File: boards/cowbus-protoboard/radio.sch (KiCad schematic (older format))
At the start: 3 parts

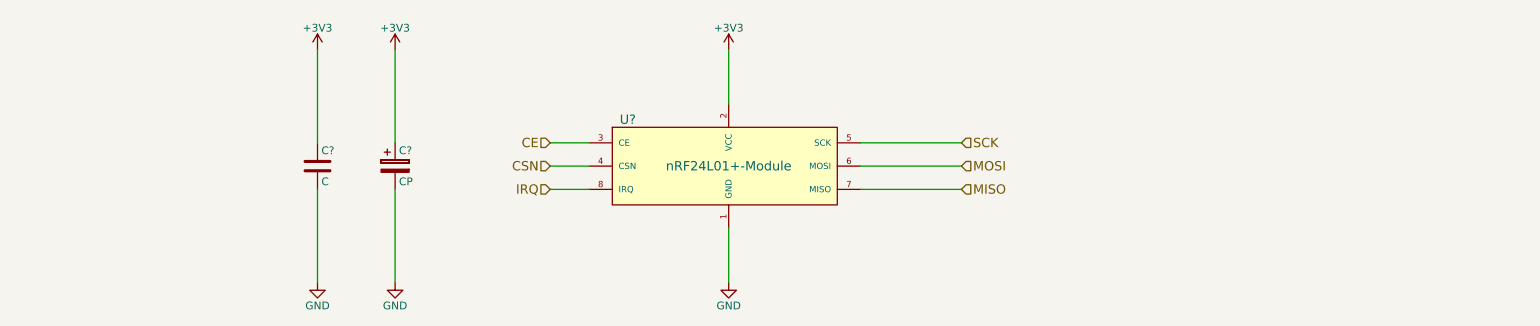
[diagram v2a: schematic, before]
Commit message: values added, 100n for uC added
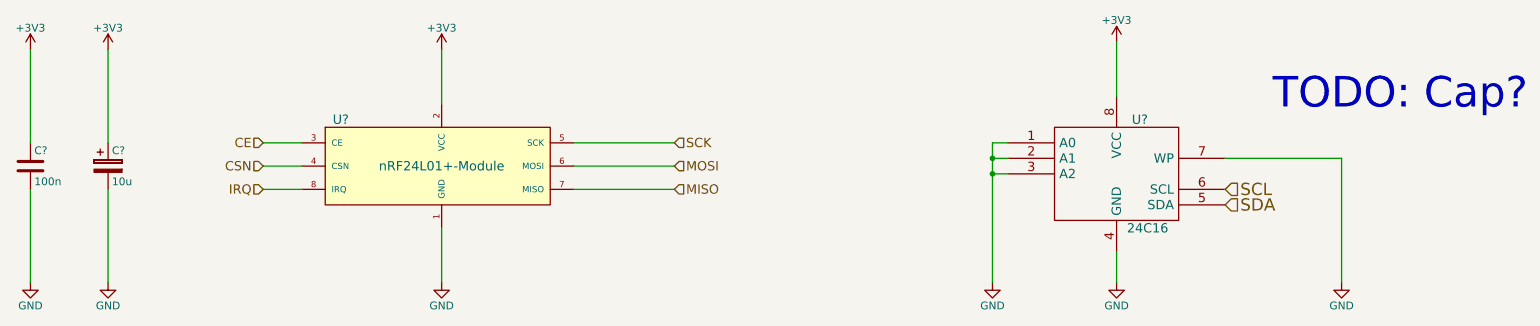
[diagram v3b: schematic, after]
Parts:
- added U?: 24C16, symbol 24C16
- C?: value C -> 100n
- C?: value CP -> 10u
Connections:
- net +3V3: now also U?.8 (VCC)
- net GND: now also U?.1 (A0), U?.2 (A1), U?.3 (A2), U?.4 (GND), U?.7 (WP)
- new net SCL: U?.6 (SCL)
- new net SDA: U?.5 (SDA)
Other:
- note added: "TODO: Cap?"
- moved on the sheet: C?, U?
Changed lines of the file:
@@
 encoding utf-8
 Sheet 4 6
-Title ""
-Date ""
-Rev ""
+Title "cowbus protoboard"
+Date "2015-07-15"
+Rev "0.9"
 Comp ""
 Comment1 ""
@@
 L nRF24L01+-Module U?
 U 1 1 55A51C3D
-P 5650 3950
-F 0 "U?" H 5000 4250 60  0000 C CNN
-F 1 "nRF24L01+-Module" H 5650 3950 60  0000 C CNN
-F 2 "" H 5750 3550 60  0000 C CNN
-F 3 "" H 5750 3550 60  0000 C CNN
-	1    5650 3950
+P 3800 3950
+F 0 "U?" H 3150 4250 60  0000 C CNN
+F 1 "nRF24L01+-Module" H 3800 3950 60  0000 C CNN
+F 2 "" H 3900 3550 60  0000 C CNN
+F 3 "" H 3900 3550 60  0000 C CNN
+	1    3800 3950
 	1    0    0    -1
 $EndComp
@@
 L GND #PWR?
 U 1 1 55A51C67
-P 5650 4700
-F 0 "#PWR?" H 5650 4450 50  0001 C CNN
-F 1 "GND" H 5650 4550 50  0000 C CNN
-F 2 "" H 5650 4700 60  0000 C CNN
-F 3 "" H 5650 4700 60  0000 C CNN
-	1    5650 4700
+P 3800 4700
+F 0 "#PWR?" H 3800 4450 50  0001 C CNN
+F 1 "GND" H 3800 4550 50  0000 C CNN
+F 2 "" H 3800 4700 60  0000 C CNN
+F 3 "" H 3800 4700 60  0000 C CNN
+	1    3800 4700
 	1    0    0    -1
 $EndComp
@@
 L +3V3 #PWR?
 U 1 1 55A51C7D
-P 5650 3200
-F 0 "#PWR?" H 5650 3050 50  0001 C CNN
-F 1 "+3V3" H 5650 3340 50  0000 C CNN
-F 2 "" H 5650 3200 60  0000 C CNN
-F 3 "" H 5650 3200 60  0000 C CNN
-	1    5650 3200
-	1    0    0    -1
-$EndComp
-Text HLabel 7150 3800 2    60   Input ~ 0
+P 3800 3200
+F 0 "#PWR?" H 3800 3050 50  0001 C CNN
+F 1 "+3V3" H 3800 3340 50  0000 C CNN
+F 2 "" H 3800 3200 60  0000 C CNN
+F 3 "" H 3800 3200 60  0000 C CNN
+	1    3800 3200
+	1    0    0    -1
+$EndComp
+Text HLabel 5300 3800 2    60   Input ~ 0
 SCK
 Wire Wire Line
-	5650 3550 5650 3200
-Wire Wire Line
-	5650 4350 5650 4700
-Wire Wire Line
-	6500 3800 7150 3800
-Wire Wire Line
-	6500 3950 7150 3950
-Wire Wire Line
-	6500 4100 7150 4100
-Text HLabel 7150 3950 2    60   Input ~ 0
+	3800 3550 3800 3200
+Wire Wire Line
+	3800 4350 3800 4700
+Wire Wire Line
+	4650 3800 5300 3800
+Wire Wire Line
+	4650 3950 5300 3950
+Wire Wire Line
+	4650 4100 5300 4100
+Text HLabel 5300 3950 2    60   Input ~ 0
 MOSI
-Text HLabel 7150 4100 2    60   Input ~ 0
+Text HLabel 5300 4100 2    60   Input ~ 0
 MISO
 Wire Wire Line
-	4750 3800 4500 3800
-Wire Wire Line
-	4750 3950 4500 3950
-Wire Wire Line
-	4750 4100 4500 4100
-Text HLabel 4500 3800 0    60   Input ~ 0
+	2900 3800 2650 3800
+Wire Wire Line
+	2900 3950 2650 3950
+Wire Wire Line
+	2900 4100 2650 4100
+Text HLabel 2650 3800 0    60   Input ~ 0
 CE
-Text HLabel 4500 3950 0    60   Input ~ 0
+Text HLabel 2650 3950 0    60   Input ~ 0
 CSN
-Text HLabel 4500 4100 0    60   Input ~ 0
+Text HLabel 2650 4100 0    60   Input ~ 0
 IRQ
 $Comp
 L GND #PWR?
 U 1 1 55A72AEE
-P 3000 4700
-F 0 "#PWR?" H 3000 4450 50  0001 C CNN
-F 1 "GND" H 3000 4550 50  0000 C CNN
-F 2 "" H 3000 4700 60  0000 C CNN
-F 3 "" H 3000 4700 60  0000 C CNN
-	1    3000 4700
+P 1150 4700
+F 0 "#PWR?" H 1150 4450 50  0001 C CNN
+F 1 "GND" H 1150 4550 50  0000 C CNN
+F 2 "" H 1150 4700 60  0000 C CNN
+F 3 "" H 1150 4700 60  0000 C CNN
+	1    1150 4700
 	1    0    0    -1
 $EndComp
@@
 L +3V3 #PWR?
 U 1 1 55A72AF4
-P 3000 3200
-F 0 "#PWR?" H 3000 3050 50  0001 C CNN
-F 1 "+3V3" H 3000 3340 50  0000 C CNN
-F 2 "" H 3000 3200 60  0000 C CNN
-F 3 "" H 3000 3200 60  0000 C CNN
-	1    3000 3200
-	1    0    0    -1
-$EndComp
-Wire Wire Line
-	3000 3200 3000 3800
-Wire Wire Line
-	3000 4100 3000 4700
+P 1150 3200
+F 0 "#PWR?" H 1150 3050 50  0001 C CNN
+F 1 "+3V3" H 1150 3340 50  0000 C CNN
+F 2 "" H 1150 3200 60  0000 C CNN
+F 3 "" H 1150 3200 60  0000 C CNN
+	1    1150 3200
+	1    0    0    -1
+$EndComp
+Wire Wire Line
+	1150 3200 1150 3800
+Wire Wire Line
+	1150 4100 1150 4700
 $Comp
 L C C?
 U 1 1 55A72B04
-P 3000 3950
-F 0 "C?" H 3025 4050 50  0000 L CNN
-F 1 "C" H 3025 3850 50  0000 L CNN
-F 2 "" H 3038 3800 30  0000 C CNN
-F 3 "" H 3000 3950 60  0000 C CNN
-	1    3000 3950
+P 1150 3950
+F 0 "C?" H 1175 4050 50  0000 L CNN
+F 1 "100n" H 1175 3850 50  0000 L CNN
+F 2 "" H 1188 3800 30  0000 C CNN
+F 3 "" H 1150 3950 60  0000 C CNN
+	1    1150 3950
 	1    0    0    -1
 $EndComp
@@
 L CP C?
 U 1 1 55A72B51
-P 3500 3950
-F 0 "C?" H 3525 4050 50  0000 L CNN
-F 1 "CP" H 3525 3850 50  0000 L CNN
-F 2 "" H 3538 3800 30  0000 C CNN
-F 3 "" H 3500 3950 60  0000 C CNN
-	1    3500 3950
-	1    0    0    -1
-$EndComp
-Wire Wire Line
-	3500 3800 3500 3200
-Wire Wire Line
-	3500 4100 3500 4700
+P 1650 3950
+F 0 "C?" H 1675 4050 50  0000 L CNN
+F 1 "10u" H 1675 3850 50  0000 L CNN
+F 2 "" H 1688 3800 30  0000 C CNN
+F 3 "" H 1650 3950 60  0000 C CNN
+	1    1650 3950
+	1    0    0    -1
+$EndComp
+Wire Wire Line
+	1650 3800 1650 3200
+Wire Wire Line
+	1650 4100 1650 4700
 $Comp
 L GND #PWR?
 U 1 1 55A72BFA
-P 3500 4700
-F 0 "#PWR?" H 3500 4450 50  0001 C CNN
-F 1 "GND" H 3500 4550 50  0000 C CNN
-F 2 "" H 3500 4700 60  0000 C CNN
-F 3 "" H 3500 4700 60  0000 C CNN
-	1    3500 4700
+P 1650 4700
+F 0 "#PWR?" H 1650 4450 50  0001 C CNN
+F 1 "GND" H 1650 4550 50  0000 C CNN
+F 2 "" H 1650 4700 60  0000 C CNN
+F 3 "" H 1650 4700 60  0000 C CNN
+	1    1650 4700
 	1    0    0    -1
 $EndComp
@@
 L +3V3 #PWR?
 U 1 1 55A72C0E
-P 3500 3200
-F 0 "#PWR?" H 3500 3050 50  0001 C CNN
-F 1 "+3V3" H 3500 3340 50  0000 C CNN
-F 2 "" H 3500 3200 60  0000 C CNN
-F 3 "" H 3500 3200 60  0000 C CNN
-	1    3500 3200
-	1    0    0    -1
-$EndComp
+P 1650 3200
+F 0 "#PWR?" H 1650 3050 50  0001 C CNN
+F 1 "+3V3" H 1650 3340 50  0000 C CNN
+F 2 "" H 1650 3200 60  0000 C CNN
+F 3 "" H 1650 3200 60  0000 C CNN
+	1    1650 3200
+	1    0    0    -1
+$EndComp
+$Comp
+L 24C16 U?
+U 1 1 55A89592
+P 8150 4000
+F 0 "U?" H 8300 4350 60  0000 C CNN
+F 1 "24C16" H 8350 3650 60  0000 C CNN
+F 2 "" H 8150 4000 60  0000 C CNN
+F 3 "" H 8150 4000 60  0000 C CNN
+	1    8150 4000
+	1    0    0    -1
+$EndComp
+$Comp
+L +3V3 #PWR?
+U 1 1 55A89652
+P 8150 3150
+F 0 "#PWR?" H 8150 3000 50  0001 C CNN
+F 1 "+3V3" H 8150 3290 50  0000 C CNN
+F 2 "" H 8150 3150 60  0000 C CNN
+F 3 "" H 8150 3150 60  0000 C CNN
+	1    8150 3150
+	1    0    0    -1
+$EndComp
+Wire Wire Line
+	8150 3500 8150 3150
+$Comp
+L GND #PWR?
+U 1 1 55A89738
+P 8150 4700
+F 0 "#PWR?" H 8150 4450 50  0001 C CNN
+F 1 "GND" H 8150 4550 50  0000 C CNN
+F 2 "" H 8150 4700 60  0000 C CNN
+F 3 "" H 8150 4700 60  0000 C CNN
+	1    8150 4700
+	1    0    0    -1
+$EndComp
+Wire Wire Line
+	8150 4700 8150 4500
+Wire Wire Line
+	7450 3800 7350 3800
+Wire Wire Line
+	7350 3800 7350 4700
+Wire Wire Line
+	7450 3900 7350 3900
+Connection ~ 7350 3900
+Wire Wire Line
+	7450 4000 7350 4000
+Connection ~ 7350 4000
+$Comp
+L GND #PWR?
+U 1 1 55A89845
+P 7350 4700
+F 0 "#PWR?" H 7350 4450 50  0001 C CNN
+F 1 "GND" H 7350 4550 50  0000 C CNN
+F 2 "" H 7350 4700 60  0000 C CNN
+F 3 "" H 7350 4700 60  0000 C CNN
+	1    7350 4700
+	1    0    0    -1
+$EndComp
+Wire Wire Line
+	8850 3900 9600 3900
+$Comp
+L GND #PWR?
+U 1 1 55A8993F
+P 9600 4700
+F 0 "#PWR?" H 9600 4450 50  0001 C CNN
+F 1 "GND" H 9600 4550 50  0000 C CNN
+F 2 "" H 9600 4700 60  0000 C CNN
+F 3 "" H 9600 4700 60  0000 C CNN
+	1    9600 4700
+	1    0    0    -1
+$EndComp
+Wire Wire Line
+	9600 3900 9600 4700
+Text HLabel 8850 4100 2    79   Input ~ 0
+SCL
+Text HLabel 8850 4200 2    79   Input ~ 0
+SDA
+Text Notes 10800 3600 2    197  ~ 0
+TODO: Cap?
 $EndSCHEMATC

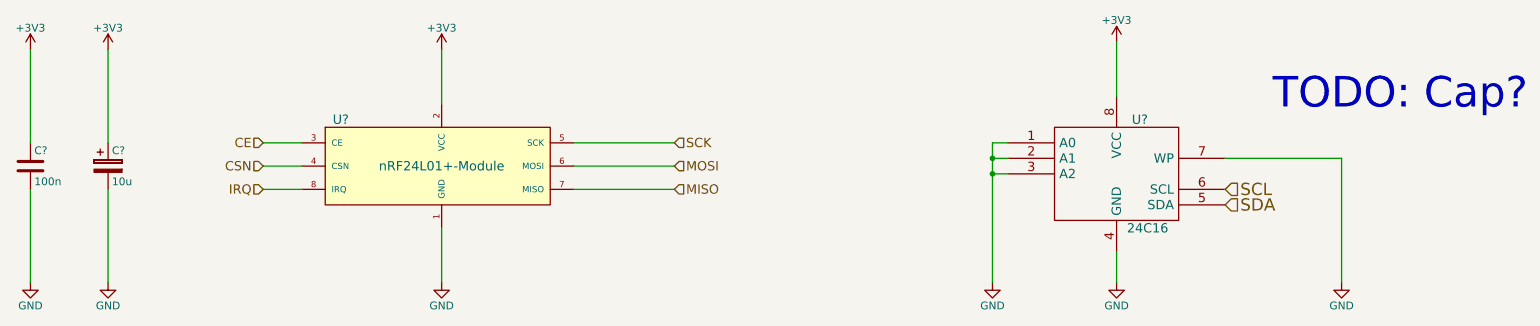
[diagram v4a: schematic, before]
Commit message: some footprint assignments done
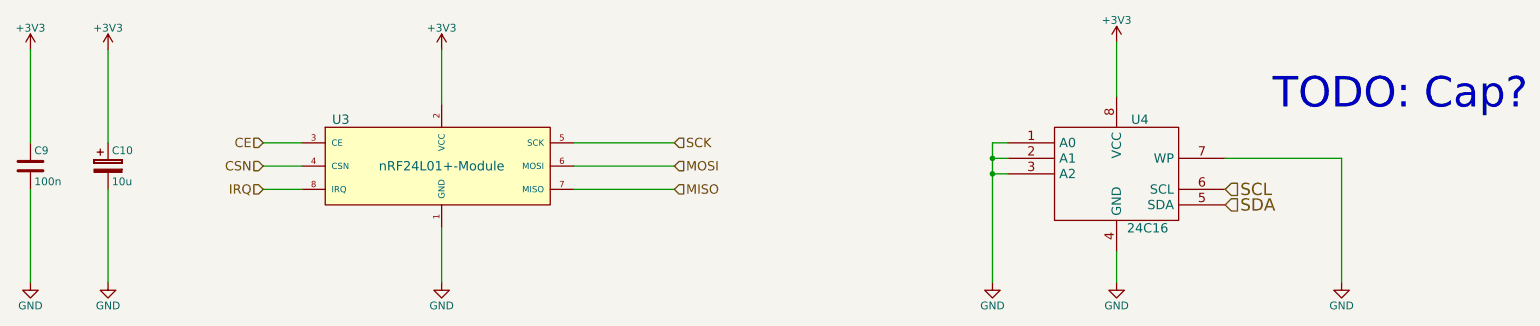
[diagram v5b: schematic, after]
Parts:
- C10: renamed from C?; footprint (none) -> Capacitors_SMD:c_elec_4x5.8
- C9: renamed from C?; footprint (none) -> Capacitors_SMD:C_0805_HandSoldering
- U3: renamed from U?; footprint (none) -> Pin_Headers:Pin_Header_Straight_2x05
- gave numbers to parts that had none: 1
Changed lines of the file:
@@
 $EndDescr
 $Comp
-L nRF24L01+-Module U?
+L nRF24L01+-Module U3
 U 1 1 55A51C3D
 P 3800 3950
-F 0 "U?" H 3150 4250 60  0000 C CNN
+F 0 "U3" H 3150 4250 60  0000 C CNN
 F 1 "nRF24L01+-Module" H 3800 3950 60  0000 C CNN
-F 2 "" H 3900 3550 60  0000 C CNN
+F 2 "Pin_Headers:Pin_Header_Straight_2x05" H 3900 3550 60  0001 C CNN
 F 3 "" H 3900 3550 60  0000 C CNN
 	1    3800 3950
@@
 $EndComp
 $Comp
-L GND #PWR?
+L GND #PWR031
 U 1 1 55A51C67
 P 3800 4700
-F 0 "#PWR?" H 3800 4450 50  0001 C CNN
+F 0 "#PWR031" H 3800 4450 50  0001 C CNN
 F 1 "GND" H 3800 4550 50  0000 C CNN
 F 2 "" H 3800 4700 60  0000 C CNN
@@
 $EndComp
 $Comp
-L +3V3 #PWR?
+L +3V3 #PWR032
 U 1 1 55A51C7D
 P 3800 3200
-F 0 "#PWR?" H 3800 3050 50  0001 C CNN
+F 0 "#PWR032" H 3800 3050 50  0001 C CNN
 F 1 "+3V3" H 3800 3340 50  0000 C CNN
 F 2 "" H 3800 3200 60  0000 C CNN
@@
 IRQ
 $Comp
-L GND #PWR?
+L GND #PWR033
 U 1 1 55A72AEE
 P 1150 4700
-F 0 "#PWR?" H 1150 4450 50  0001 C CNN
+F 0 "#PWR033" H 1150 4450 50  0001 C CNN
 F 1 "GND" H 1150 4550 50  0000 C CNN
 F 2 "" H 1150 4700 60  0000 C CNN
@@
 $EndComp
 $Comp
-L +3V3 #PWR?
+L +3V3 #PWR034
 U 1 1 55A72AF4
 P 1150 3200
-F 0 "#PWR?" H 1150 3050 50  0001 C CNN
+F 0 "#PWR034" H 1150 3050 50  0001 C CNN
 F 1 "+3V3" H 1150 3340 50  0000 C CNN
 F 2 "" H 1150 3200 60  0000 C CNN
@@
 	1150 4100 1150 4700
 $Comp
-L C C?
+L C C9
 U 1 1 55A72B04
 P 1150 3950
-F 0 "C?" H 1175 4050 50  0000 L CNN
+F 0 "C9" H 1175 4050 50  0000 L CNN
 F 1 "100n" H 1175 3850 50  0000 L CNN
-F 2 "" H 1188 3800 30  0000 C CNN
+F 2 "Capacitors_SMD:C_0805_HandSoldering" H 1188 3800 30  0001 C CNN
 F 3 "" H 1150 3950 60  0000 C CNN
 	1    1150 3950
@@
 $EndComp
 $Comp
-L CP C?
+L CP C10
 U 1 1 55A72B51
 P 1650 3950
-F 0 "C?" H 1675 4050 50  0000 L CNN
+F 0 "C10" H 1675 4050 50  0000 L CNN
 F 1 "10u" H 1675 3850 50  0000 L CNN
-F 2 "" H 1688 3800 30  0000 C CNN
+F 2 "Capacitors_SMD:c_elec_4x5.8" H 1688 3800 30  0001 C CNN
 F 3 "" H 1650 3950 60  0000 C CNN
 	1    1650 3950
@@
 	1650 4100 1650 4700
 $Comp
-L GND #PWR?
+L GND #PWR035
 U 1 1 55A72BFA
 P 1650 4700
-F 0 "#PWR?" H 1650 4450 50  0001 C CNN
+F 0 "#PWR035" H 1650 4450 50  0001 C CNN
 F 1 "GND" H 1650 4550 50  0000 C CNN
 F 2 "" H 1650 4700 60  0000 C CNN
@@
 $EndComp
 $Comp
-L +3V3 #PWR?
+L +3V3 #PWR036
 U 1 1 55A72C0E
 P 1650 3200
-F 0 "#PWR?" H 1650 3050 50  0001 C CNN
+F 0 "#PWR036" H 1650 3050 50  0001 C CNN
 F 1 "+3V3" H 1650 3340 50  0000 C CNN
 F 2 "" H 1650 3200 60  0000 C CNN
@@
 $EndComp
 $Comp
-L 24C16 U?
+L 24C16 U4
 U 1 1 55A89592
 P 8150 4000
-F 0 "U?" H 8300 4350 60  0000 C CNN
+F 0 "U4" H 8300 4350 60  0000 C CNN
 F 1 "24C16" H 8350 3650 60  0000 C CNN
-F 2 "" H 8150 4000 60  0000 C CNN
+F 2 "" H 8150 4000 60  0001 C CNN
 F 3 "" H 8150 4000 60  0000 C CNN
 	1    8150 4000
@@
 $EndComp
 $Comp
-L +3V3 #PWR?
+L +3V3 #PWR037
 U 1 1 55A89652
 P 8150 3150
-F 0 "#PWR?" H 8150 3000 50  0001 C CNN
+F 0 "#PWR037" H 8150 3000 50  0001 C CNN
 F 1 "+3V3" H 8150 3290 50  0000 C CNN
 F 2 "" H 8150 3150 60  0000 C CNN
@@
 	8150 3500 8150 3150
 $Comp
-L GND #PWR?
+L GND #PWR038
 U 1 1 55A89738
 P 8150 4700
-F 0 "#PWR?" H 8150 4450 50  0001 C CNN
+F 0 "#PWR038" H 8150 4450 50  0001 C CNN
 F 1 "GND" H 8150 4550 50  0000 C CNN
 F 2 "" H 8150 4700 60  0000 C CNN
@@
 Connection ~ 7350 4000
 $Comp
-L GND #PWR?
+L GND #PWR039
 U 1 1 55A89845
 P 7350 4700
-F 0 "#PWR?" H 7350 4450 50  0001 C CNN
+F 0 "#PWR039" H 7350 4450 50  0001 C CNN
 F 1 "GND" H 7350 4550 50  0000 C CNN
 F 2 "" H 7350 4700 60  0000 C CNN
@@
 	8850 3900 9600 3900
 $Comp
-L GND #PWR?
+L GND #PWR040
 U 1 1 55A8993F
 P 9600 4700
-F 0 "#PWR?" H 9600 4450 50  0001 C CNN
+F 0 "#PWR040" H 9600 4450 50  0001 C CNN
 F 1 "GND" H 9600 4550 50  0000 C CNN
 F 2 "" H 9600 4700 60  0000 C CNN

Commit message: first version of layout for protoboard
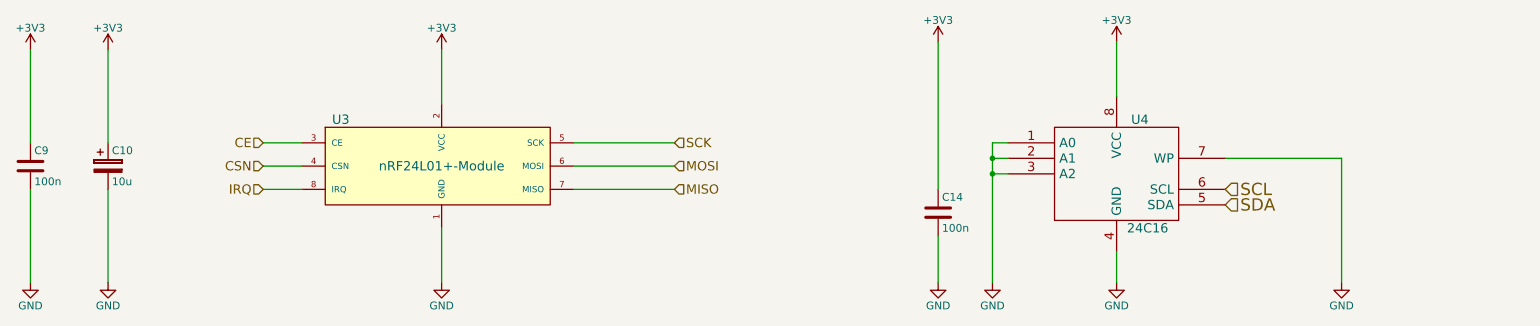
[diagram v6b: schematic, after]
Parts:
- added C14: 100n, Capacitors_SMD:C_0805_HandSoldering, symbol C
- U4: footprint (none) -> SMD_Packages:SOIC-8-N
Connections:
- net +3V3: now also C14.1
- net GND: now also C14.2
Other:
- note removed: "TODO: Cap?"
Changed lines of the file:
@@
 EESchema Schematic File Version 2
+LIBS:cowbus-protoboard-rescue
 LIBS:power
 LIBS:device
@@
 LIBS:nrf24l01plus-module
 LIBS:i2c
+LIBS:led_rgb_reichelt
 LIBS:cowbus-protoboard-cache
 EELAYER 25 0
@@
 $EndComp
 $Comp
-L GND #PWR031
+L GND #PWR43
 U 1 1 55A51C67
 P 3800 4700
-F 0 "#PWR031" H 3800 4450 50  0001 C CNN
+F 0 "#PWR43" H 3800 4450 50  0001 C CNN
 F 1 "GND" H 3800 4550 50  0000 C CNN
 F 2 "" H 3800 4700 60  0000 C CNN
@@
 $EndComp
 $Comp
-L +3V3 #PWR032
+L +3V3 #PWR42
 U 1 1 55A51C7D
 P 3800 3200
-F 0 "#PWR032" H 3800 3050 50  0001 C CNN
+F 0 "#PWR42" H 3800 3050 50  0001 C CNN
 F 1 "+3V3" H 3800 3340 50  0000 C CNN
 F 2 "" H 3800 3200 60  0000 C CNN
@@
 IRQ
 $Comp
-L GND #PWR033
+L GND #PWR39
 U 1 1 55A72AEE
 P 1150 4700
-F 0 "#PWR033" H 1150 4450 50  0001 C CNN
+F 0 "#PWR39" H 1150 4450 50  0001 C CNN
 F 1 "GND" H 1150 4550 50  0000 C CNN
 F 2 "" H 1150 4700 60  0000 C CNN
@@
 $EndComp
 $Comp
-L +3V3 #PWR034
+L +3V3 #PWR38
 U 1 1 55A72AF4
 P 1150 3200
-F 0 "#PWR034" H 1150 3050 50  0001 C CNN
+F 0 "#PWR38" H 1150 3050 50  0001 C CNN
 F 1 "+3V3" H 1150 3340 50  0000 C CNN
 F 2 "" H 1150 3200 60  0000 C CNN
@@
 	1650 4100 1650 4700
 $Comp
-L GND #PWR035
+L GND #PWR41
 U 1 1 55A72BFA
 P 1650 4700
-F 0 "#PWR035" H 1650 4450 50  0001 C CNN
+F 0 "#PWR41" H 1650 4450 50  0001 C CNN
 F 1 "GND" H 1650 4550 50  0000 C CNN
 F 2 "" H 1650 4700 60  0000 C CNN
@@
 $EndComp
 $Comp
-L +3V3 #PWR036
+L +3V3 #PWR40
 U 1 1 55A72C0E
 P 1650 3200
-F 0 "#PWR036" H 1650 3050 50  0001 C CNN
+F 0 "#PWR40" H 1650 3050 50  0001 C CNN
 F 1 "+3V3" H 1650 3340 50  0000 C CNN
 F 2 "" H 1650 3200 60  0000 C CNN
@@
 F 0 "U4" H 8300 4350 60  0000 C CNN
 F 1 "24C16" H 8350 3650 60  0000 C CNN
-F 2 "" H 8150 4000 60  0001 C CNN
+F 2 "SMD_Packages:SOIC-8-N" H 8150 4000 60  0001 C CNN
 F 3 "" H 8150 4000 60  0000 C CNN
 	1    8150 4000
@@
 $EndComp
 $Comp
-L +3V3 #PWR037
+L +3V3 #PWR47
 U 1 1 55A89652
 P 8150 3150
-F 0 "#PWR037" H 8150 3000 50  0001 C CNN
+F 0 "#PWR47" H 8150 3000 50  0001 C CNN
 F 1 "+3V3" H 8150 3290 50  0000 C CNN
 F 2 "" H 8150 3150 60  0000 C CNN
@@
 	8150 3500 8150 3150
 $Comp
-L GND #PWR038
+L GND #PWR48
 U 1 1 55A89738
 P 8150 4700
-F 0 "#PWR038" H 8150 4450 50  0001 C CNN
+F 0 "#PWR48" H 8150 4450 50  0001 C CNN
 F 1 "GND" H 8150 4550 50  0000 C CNN
 F 2 "" H 8150 4700 60  0000 C CNN
@@
 Connection ~ 7350 4000
 $Comp
-L GND #PWR039
+L GND #PWR46
 U 1 1 55A89845
 P 7350 4700
-F 0 "#PWR039" H 7350 4450 50  0001 C CNN
+F 0 "#PWR46" H 7350 4450 50  0001 C CNN
 F 1 "GND" H 7350 4550 50  0000 C CNN
 F 2 "" H 7350 4700 60  0000 C CNN
@@
 	8850 3900 9600 3900
 $Comp
-L GND #PWR040
+L GND #PWR49
 U 1 1 55A8993F
 P 9600 4700
-F 0 "#PWR040" H 9600 4450 50  0001 C CNN
+F 0 "#PWR49" H 9600 4450 50  0001 C CNN
 F 1 "GND" H 9600 4550 50  0000 C CNN
 F 2 "" H 9600 4700 60  0000 C CNN
@@
 Text HLabel 8850 4200 2    79   Input ~ 0
 SDA
-Text Notes 10800 3600 2    197  ~ 0
-TODO: Cap?
+$Comp
+L GND #PWR45
+U 1 1 55BE9456
+P 7000 4700
+F 0 "#PWR45" H 7000 4450 50  0001 C CNN
+F 1 "GND" H 7000 4550 50  0000 C CNN
+F 2 "" H 7000 4700 60  0000 C CNN
+F 3 "" H 7000 4700 60  0000 C CNN
+	1    7000 4700
+	1    0    0    -1
+$EndComp
+$Comp
+L +3V3 #PWR44
+U 1 1 55BE945C
+P 7000 3150
+F 0 "#PWR44" H 7000 3000 50  0001 C CNN
+F 1 "+3V3" H 7000 3290 50  0000 C CNN
+F 2 "" H 7000 3150 60  0000 C CNN
+F 3 "" H 7000 3150 60  0000 C CNN
+	1    7000 3150
+	1    0    0    -1
+$EndComp
+$Comp
+L C C14
+U 1 1 55BE9462
+P 7000 4250
+F 0 "C14" H 7025 4350 50  0000 L CNN
+F 1 "100n" H 7025 4150 50  0000 L CNN
+F 2 "Capacitors_SMD:C_0805_HandSoldering" H 7038 4100 30  0001 C CNN
+F 3 "" H 7000 4250 60  0000 C CNN
+	1    7000 4250
+	1    0    0    -1
+$EndComp
+Wire Wire Line
+	7000 3150 7000 4100
+Wire Wire Line
+	7000 4700 7000 4400
 $EndSCHEMATC
